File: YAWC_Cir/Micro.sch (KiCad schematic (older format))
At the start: 23 parts, among them P3 CONN_5, P4 CONN_5, P5 CONN_6, P7 J_AllOff, P8 J_Pot, U2 SAMD20J18A-M

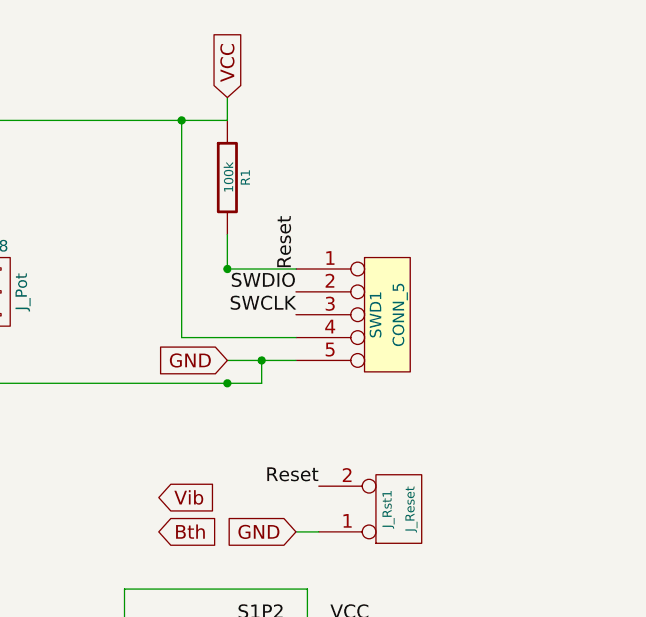
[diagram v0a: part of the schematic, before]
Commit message: move parts nearer final positions
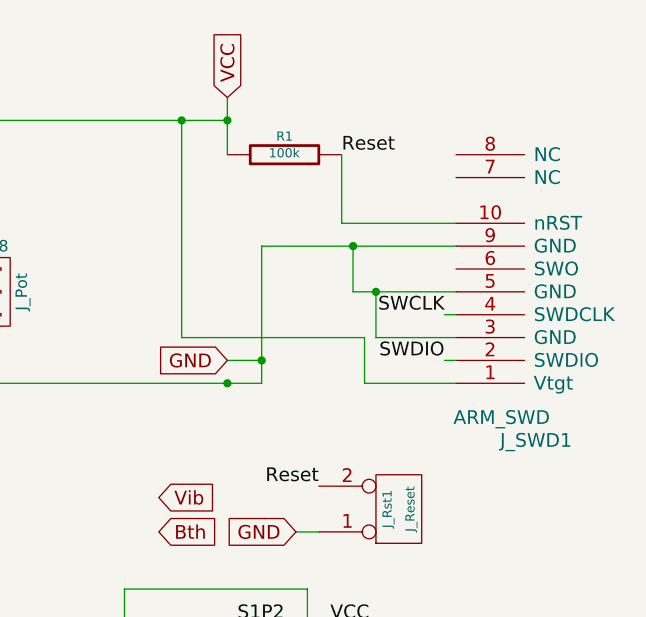
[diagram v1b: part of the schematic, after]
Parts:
- removed SWD1: CONN_5, PIN_Hdr:Pin_Header_Straight_1x05, symbol CONN_5
- added J_SWD1: ARM_SWD, My_Pin_Headers:2x5_50mil_SMD, symbol ARM_SWD
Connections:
- net GND: now also J_SWD1.3 (GND), J_SWD1.5 (GND), J_SWD1.9 (GND)
- net Reset: now also J_SWD1.10 (nRST)
- net SWCLK: now also J_SWD1.4 (SWDCLK)
- net SWDIO: now also J_SWD1.2 (SWDIO)
- net VCC: now also J_SWD1.1 (Vtgt)
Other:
- moved on the sheet: R1
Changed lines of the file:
@@
 Text Label 3850 1850 2    60   ~ 0
 Reset
-$Comp
-L CONN_5 SWD1
-U 1 1 53989F52
-P 10400 2000
-F 0 "SWD1" V 10350 2000 50  0000 C CNN
-F 1 "CONN_5" V 10450 2000 50  0000 C CNN
-F 2 "PIN_Hdr:Pin_Header_Straight_1x05" H 10400 2000 60  0001 C CNN
-F 3 "" H 10400 2000 60  0000 C CNN
-	1    10400 2000
-	1    0    0    -1
-$EndComp
 Text GLabel 9700 1050 1    60   Input ~ 0
 VCC
@@
 L R-RESCUE-YAWC R1
 U 1 1 53989FCC
-P 9700 1400
-F 0 "R1" V 9780 1400 40  0000 C CNN
-F 1 "100k" V 9707 1401 40  0000 C CNN
-F 2 "Resistors_SMD:R_0805_HandSoldering" V 9630 1400 30  0001 C CNN
-F 3 "" H 9700 1400 30  0000 C CNN
-	1    9700 1400
-	1    0    0    -1
-$EndComp
-Text Label 10000 1800 1    60   ~ 0
-Reset
+P 9950 1300
+F 0 "R1" V 10030 1300 40  0000 C CNN
+F 1 "100k" V 9957 1301 40  0000 C CNN
+F 2 "Resistors_SMD:R_0805_HandSoldering" V 9880 1300 30  0001 C CNN
+F 3 "" H 9950 1300 30  0000 C CNN
+	1    9950 1300
+	0    -1   -1   0
+$EndComp
 Text Label 7550 4650 0    60   ~ 0
 SWCLK
 Text Label 7550 4750 0    60   ~ 0
 SWDIO
-Text Label 10000 1900 2    60   ~ 0
+Text Label 10650 2200 2    60   ~ 0
 SWDIO
-Text Label 10000 2000 2    60   ~ 0
+Text Label 10650 2000 2    60   ~ 0
 SWCLK
 Text GLabel 9700 2200 0    60   Input ~ 0
@@
 	5300 1300 5300 1550
 Wire Wire Line
-	9700 1150 9700 1050
-Wire Wire Line
-	9700 1650 9700 1800
-Connection ~ 9700 1800
-Wire Wire Line
-	9700 1800 10000 1800
-Wire Wire Line
-	9700 2200 10000 2200
-Wire Wire Line
-	10000 2100 9500 2100
+	9700 1050 9700 1300
+Wire Wire Line
+	9500 2100 10300 2100
 Wire Wire Line
 	9500 2100 9500 1150
@@
 	10150 4300 10250 4300
 Wire Wire Line
-	9850 2300 9850 2200
+	9850 2300 9850 1700
 Connection ~ 9850 2200
 Wire Wire Line
@@
 Wire Wire Line
 	10000 2950 10100 2950
+$Comp
+L ARM_SWD J_SWD1
+U 1 1 56F1158D
+P 10900 1950
+F 0 "J_SWD1" H 10750 2550 60  0000 C CNN
+F 1 "ARM_SWD" H 10900 2450 60  0000 C CNN
+F 2 "My_Pin_Headers:2x5_50mil_SMD" H 10900 1950 60  0001 C CNN
+F 3 "" H 10900 1950 60  0000 C CNN
+	1    10900 1950
+	-1   0    0    1
+$EndComp
+Connection ~ 9700 1150
+Wire Wire Line
+	10200 1300 10200 1600
+Wire Wire Line
+	10200 1600 10700 1600
+Text Label 10200 1300 0    60   ~ 0
+Reset
+Wire Wire Line
+	10300 2100 10300 2300
+Wire Wire Line
+	10300 2300 10700 2300
+Wire Wire Line
+	9850 2200 9700 2200
+Wire Wire Line
+	9850 1700 10700 1700
+Connection ~ 10250 1700
+Wire Wire Line
+	10250 1700 10250 1900
+Wire Wire Line
+	10250 1900 10700 1900
+Wire Wire Line
+	10350 2100 10700 2100
+Wire Wire Line
+	10350 2100 10350 1900
+Connection ~ 10350 1900
+Wire Wire Line
+	10700 2000 10650 2000
+Wire Wire Line
+	10700 2200 10650 2200
 $EndSCHEMATC

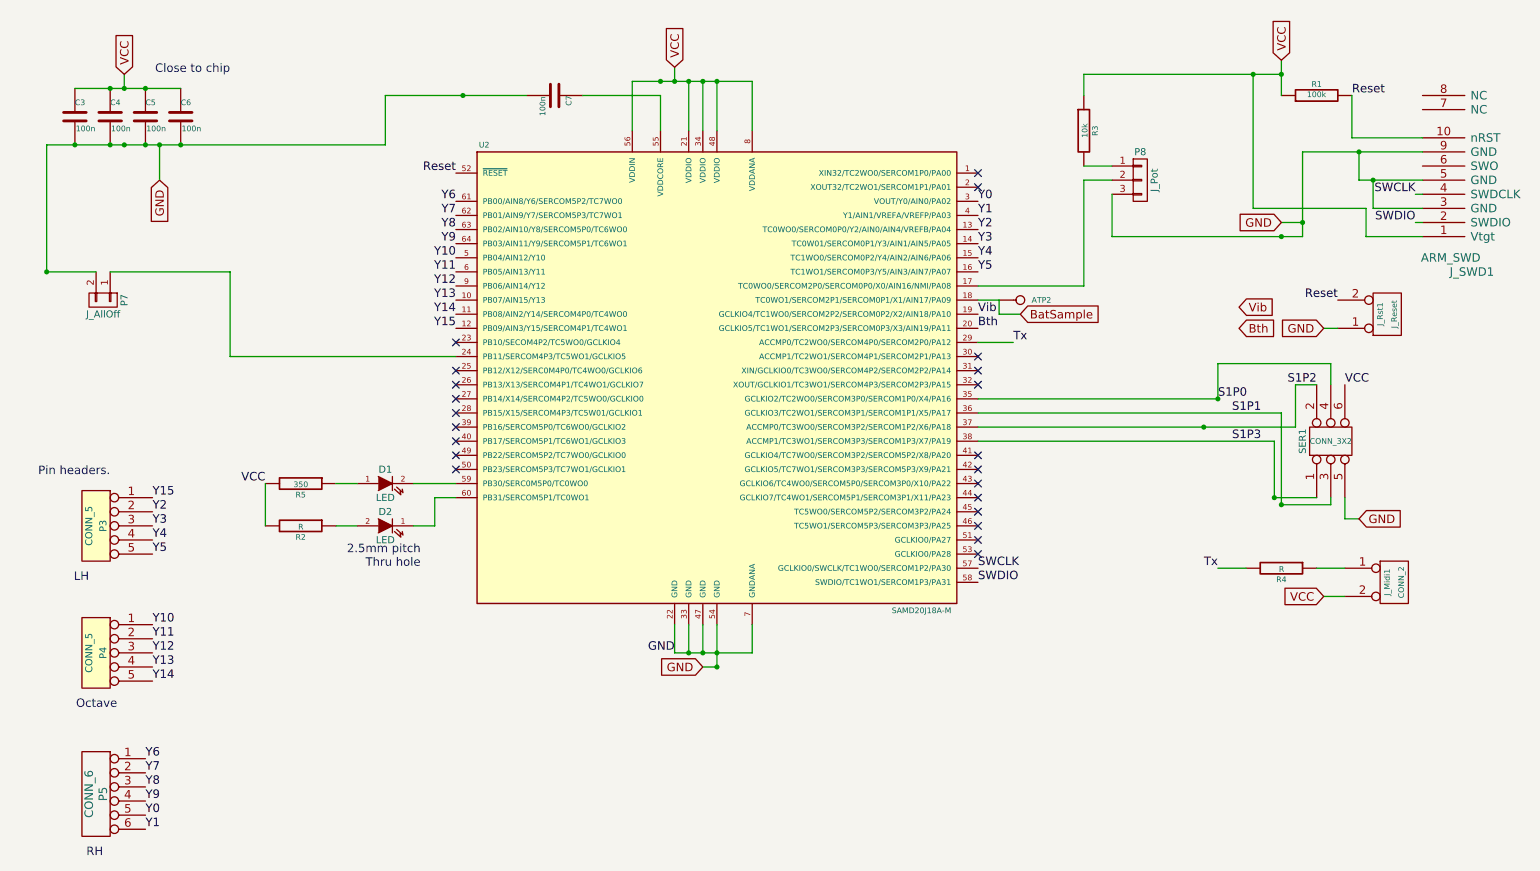
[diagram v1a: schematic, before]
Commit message: Routed but no copper pour
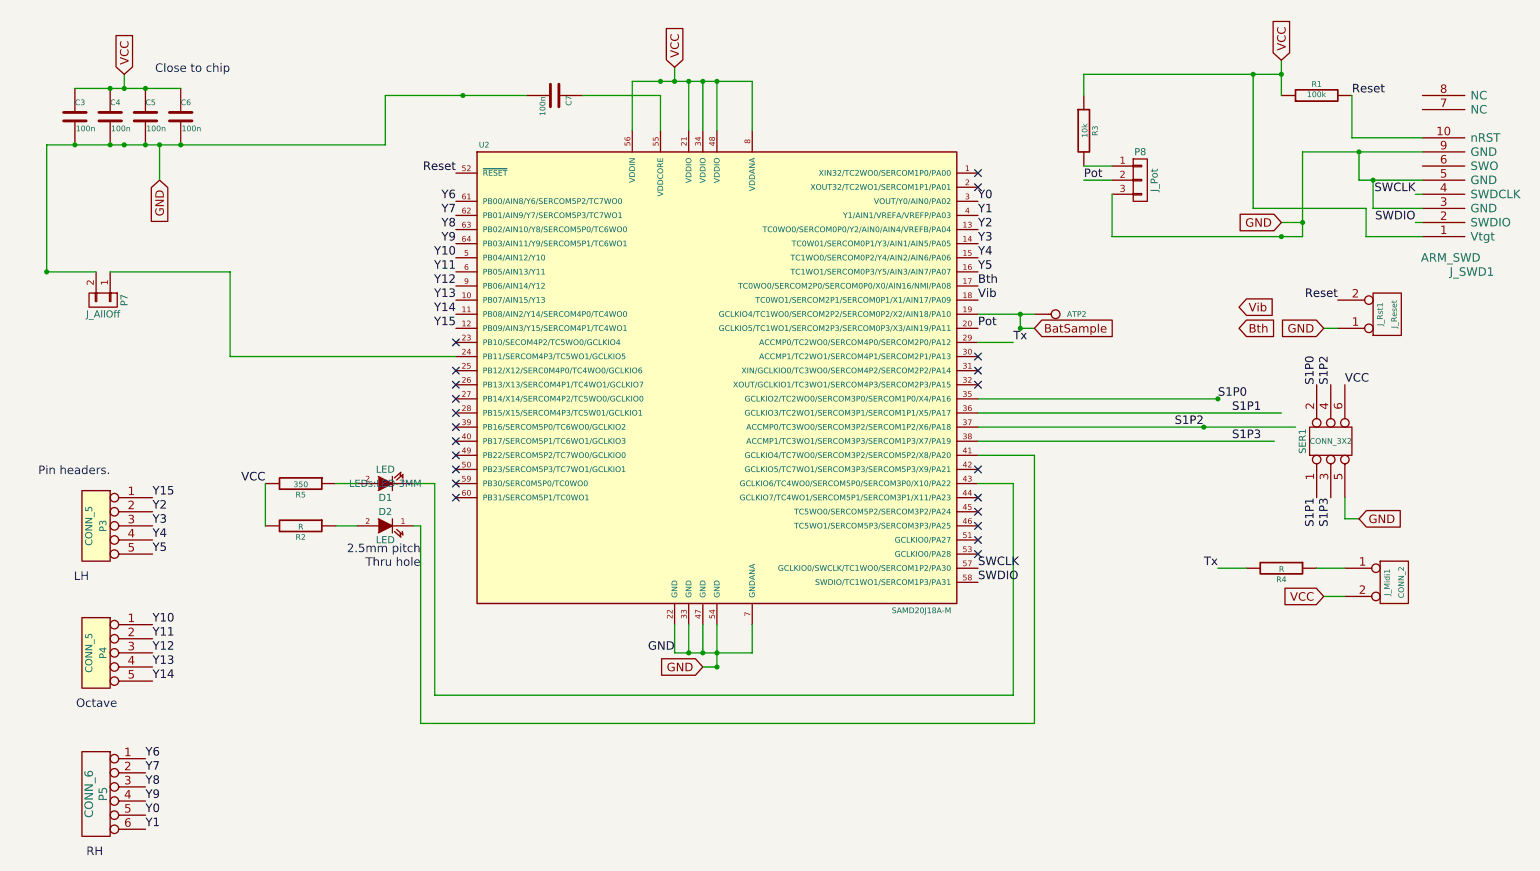
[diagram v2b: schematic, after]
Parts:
- removed D1: LED, LEDs:LED-3MM, symbol LED-RESCUE-YAWC
- added D1: LED, LEDs:LED-3MM, symbol LED
- J_Rst1, P7: footprint JST:S2B-XH -> JST:B2B-XH
- P8: footprint JST:S3B-XH -> JST:B3B-XH
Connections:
- net labels added: Pot
- wire segments 82 -> 76
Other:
- moved on the sheet: ATP2
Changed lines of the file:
@@
 Text GLabel 9700 2200 0    60   Input ~ 0
 GND
-Text Label 7550 2850 0    60   ~ 0
+Text Label 7550 2750 0    60   ~ 0
 Vib
-Text Label 7550 2950 0    60   ~ 0
+Text Label 7550 2650 0    60   ~ 0
 Bth
 Text GLabel 9400 2800 2    60   Input ~ 0
@@
 F 0 "J_Rst1" V 10400 2850 40  0000 C CNN
 F 1 "J_Reset" V 10500 2850 40  0000 C CNN
-F 2 "JST:S2B-XH" H 10450 2850 60  0001 C CNN
+F 2 "JST:B2B-XH" H 10450 2850 60  0001 C CNN
 F 3 "" H 10450 2850 60  0000 C CNN
 	1    10450 2850
@@
 	7550 3550 9700 3550
 Wire Wire Line
-	7550 3650 9800 3650
-Wire Wire Line
-	10050 4200 10050 4150
-Wire Wire Line
 	7550 3750 9650 3750
-Wire Wire Line
-	10050 3200 10050 3350
 Text Label 10150 3350 0    60   ~ 0
 VCC
@@
 Text Label 9350 3550 0    60   ~ 0
 S1P1
-Text Label 9950 3350 2    60   ~ 0
+Text Label 9150 3650 2    60   ~ 0
 S1P2
 Text Label 9350 3750 0    60   ~ 0
@@
 L CONN_1 ATP2
 U 1 1 539ECD77
-P 7850 2750
-F 0 "ATP2" H 7930 2750 40  0000 L CNN
-F 1 "CONN_1" H 7850 2805 30  0001 C CNN
-F 2 "PIN_Hdr:Pin_Header_Straight_1x01" H 7850 2750 60  0001 C CNN
-F 3 "" H 7850 2750 60  0000 C CNN
-	1    7850 2750
+P 8100 2850
+F 0 "ATP2" H 8180 2850 40  0000 L CNN
+F 1 "CONN_1" H 8100 2905 30  0001 C CNN
+F 2 "PIN_Hdr:Pin_Header_Straight_1x01" H 8100 2850 60  0001 C CNN
+F 3 "" H 8100 2850 60  0000 C CNN
+	1    8100 2850
 	1    0    0    -1
 $EndComp
-Wire Wire Line
-	7550 2650 8300 2650
-Wire Wire Line
-	7700 2750 7550 2750
-$Comp
-L LED-RESCUE-YAWC D1
-U 1 1 539ED0A8
-P 3350 4050
-F 0 "D1" H 3350 4150 50  0000 C CNN
-F 1 "LED" H 3350 3950 50  0000 C CNN
-F 2 "LEDs:LED-3MM" H 3350 4050 60  0001 C CNN
-F 3 "" H 3350 4050 60  0000 C CNN
-	1    3350 4050
-	1    0    0    -1
-$EndComp
-Wire Wire Line
-	3550 4050 3850 4050
 $Comp
 L R-RESCUE-YAWC R5
@@
 NoConn ~ 7550 4550
 NoConn ~ 7550 3950
-NoConn ~ 7550 3850
 NoConn ~ 7550 3350
 NoConn ~ 7550 3250
@@
 Connection ~ 5600 5250
 Connection ~ 5700 5250
-Wire Wire Line
-	7700 2750 7700 2850
-Wire Wire Line
-	7700 2850 7850 2850
-Text GLabel 7850 2850 2    60   Input ~ 0
+Text GLabel 7950 2950 2    60   Input ~ 0
 BatSample
-Wire Wire Line
-	9650 3750 9650 4150
-Connection ~ 9650 4150
-Wire Wire Line
-	9650 4150 9950 4150
-Wire Wire Line
-	9250 3200 10050 3200
 Connection ~ 9250 3450
-Wire Wire Line
-	9250 3450 9250 3200
-Wire Wire Line
-	9700 3550 9700 4200
-Connection ~ 9700 4200
-Wire Wire Line
-	9700 4200 10050 4200
-Wire Wire Line
-	9800 3650 9800 3350
-Wire Wire Line
-	9800 3350 9950 3350
 Connection ~ 9150 3650
 Text GLabel 10000 4850 0    60   Input ~ 0
@@
 Wire Wire Line
 	3000 4350 3150 4350
-Wire Wire Line
-	3550 4350 3700 4350
-Wire Wire Line
-	3700 4350 3700 4150
-Wire Wire Line
-	3700 4150 3850 4150
 Text Notes 3600 4650 2    60   ~ 0
 2.5mm pitch\nThru hole
@@
 F 0 "P8" H 8700 2100 50  0000 C CNN
 F 1 "J_Pot" V 8800 1900 50  0000 C CNN
-F 2 "JST:S3B-XH" H 8700 1900 50  0001 C CNN
+F 2 "JST:B3B-XH" H 8700 1900 50  0001 C CNN
 F 3 "" H 8700 1900 50  0000 C CNN
 	1    8700 1900
@@
 	8300 1800 8500 1800
 Wire Wire Line
-	8300 2650 8300 1900
-Wire Wire Line
 	8300 1900 8500 1900
 Wire Wire Line
@@
 F 0 "P7" H 1350 2900 50  0000 C CNN
 F 1 "J_AllOff" V 1450 2750 50  0000 C CNN
-F 2 "JST:S2B-XH" H 1350 2750 50  0001 C CNN
+F 2 "JST:B2B-XH" H 1350 2750 50  0001 C CNN
 F 3 "" H 1350 2750 50  0000 C CNN
 	1    1350 2750
@@
 NoConn ~ 3850 3350
 NoConn ~ 3850 3450
-NoConn ~ 7550 4050
 NoConn ~ 7550 4150
 Text GLabel 5600 5350 0    60   Input ~ 0
@@
 Wire Wire Line
 	10700 2200 10650 2200
+Wire Wire Line
+	7550 2850 7950 2850
+Wire Wire Line
+	7850 2850 7850 2950
+Connection ~ 7850 2950
+Wire Wire Line
+	7850 2950 7950 2950
+Connection ~ 7850 2850
+Text Label 8300 1900 0    60   ~ 0
+Pot
+Text Label 7550 2950 0    60   ~ 0
+Pot
+$Comp
+L LED D1
+U 1 1 56F906CE
+P 3350 4050
+F 0 "D1" H 3350 4150 50  0000 C CNN
+F 1 "LED" H 3350 3950 50  0000 C CNN
+F 2 "LEDs:LED-3MM" H 3350 4050 50  0000 C CNN
+F 3 "" H 3350 4050 50  0000 C CNN
+	1    3350 4050
+	-1   0    0    1
+$EndComp
+Text Label 9950 3350 1    60   ~ 0
+S1P0
+Wire Wire Line
+	7550 3650 9800 3650
+Text Label 9950 4150 3    60   ~ 0
+S1P1
+Text Label 10050 3350 1    60   ~ 0
+S1P2
+Text Label 10050 4150 3    60   ~ 0
+S1P3
+Wire Wire Line
+	3550 4350 3600 4350
+Wire Wire Line
+	3600 4350 3600 5750
+Wire Wire Line
+	3600 5750 7950 5750
+Wire Wire Line
+	7950 5750 7950 3850
+Wire Wire Line
+	7950 3850 7550 3850
+Wire Wire Line
+	3550 4050 3700 4050
+Wire Wire Line
+	3700 4050 3700 5550
+Wire Wire Line
+	3700 5550 7800 5550
+Wire Wire Line
+	7800 5550 7800 4050
+Wire Wire Line
+	7800 4050 7550 4050
+NoConn ~ 3850 4050
+NoConn ~ 3850 4150
 $EndSCHEMATC
